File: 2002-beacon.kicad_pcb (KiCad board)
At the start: 2 copper layers, 38.1 x 41.3 mm, 16 parts, among them J3 Barrel_Jack, Q1 2N3904, SW1 SW_SPST, U1 L7805, U2 ATtiny85-20PU

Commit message: fixed routing
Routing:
- net Net-(C1-Pad1): track 7.66 -> 14.0 mm
- net Net-(R2-Pad2): track 29.4 -> 25.7 mm
- net GND: track 0.00 -> 3.60 mm
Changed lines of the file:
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@@
     (thickness 1.6)
     (drawings 5)
-    (tracks 40)
+    (tracks 45)
     (zones 0)
     (modules 16)
@@
   (gr_line (start 128.905 95.885) (end 128.905 54.61) (layer Edge.Cuts) (width 0.05))
   (gr_line (start 91.44 95.885) (end 128.905 95.885) (layer Edge.Cuts) (width 0.05))
-  (segment (start 110.5536 72.39) (end 111.76 72.39) (width 0.4064) (layer F.Cu) (net 1))
-  (segment (start 108.7836 72.39) (end 110.5536 72.39) (width 0.4064) (layer F.Cu) (net 1))
-  (segment (start 106.68 70.2864) (end 108.7836 72.39) (width 0.4064) (layer F.Cu) (net 1))
-  (segment (start 106.68 68.58) (end 106.68 70.2864) (width 0.4064) (layer F.Cu) (net 1))
+  (segment (start 110.5536 72.39) (end 111.76 72.39) (width 0.8) (layer F.Cu) (net 1))
+  (segment (start 108.7836 72.39) (end 110.5536 72.39) (width 0.8) (layer F.Cu) (net 1))
+  (segment (start 106.68 70.2864) (end 108.7836 72.39) (width 0.8) (layer F.Cu) (net 1))
+  (segment (start 106.68 68.58) (end 106.68 70.2864) (width 0.8) (layer F.Cu) (net 1))
+  (segment (start 111.76 72.39) (end 111.76 78.74) (width 0.8) (layer F.Cu) (net 1))
+  (segment (start 113.76 71.25863) (end 113.284 70.78263) (width 0.5) (layer F.Cu) (net 2))
+  (segment (start 113.76 72.39) (end 113.76 71.25863) (width 0.5) (layer F.Cu) (net 2))
+  (segment (start 113.76 73.52137) (end 113.792 73.55337) (width 0.5) (layer F.Cu) (net 2))
+  (segment (start 113.76 72.39) (end 113.76 73.52137) (width 0.5) (layer F.Cu) (net 2))
+  (segment (start 113.76 73.52137) (end 113.76 74.136) (width 0.5) (layer F.Cu) (net 2))
   (segment (start 111.76 88.9636) (end 111.76 83.82) (width 0.8) (layer F.Cu) (net 3))
   (segment (start 111.76 90.17) (end 111.76 88.9636) (width 0.8) (layer F.Cu) (net 3))
@@
   (segment (start 120.65 75.565) (end 118.11 73.025) (width 0.4064) (layer F.Cu) (net 8))
   (segment (start 120.65 78.105) (end 120.65 75.565) (width 0.4064) (layer F.Cu) (net 8))
-  (segment (start 114.963201 80.038201) (end 114.963201 77.498201) (width 0.4064) (layer F.Cu) (net 9))
-  (segment (start 104.775 64.77) (end 107.315 62.23) (width 0.4064) (layer F.Cu) (net 9))
-  (segment (start 118.11 83.185) (end 114.963201 80.038201) (width 0.4064) (layer F.Cu) (net 9))
-  (segment (start 114.963201 77.498201) (end 113.665 76.2) (width 0.4064) (layer F.Cu) (net 9))
-  (segment (start 113.665 76.2) (end 110.49 76.2) (width 0.4064) (layer F.Cu) (net 9))
-  (segment (start 104.775 70.485) (end 104.775 64.77) (width 0.4064) (layer F.Cu) (net 9))
-  (segment (start 110.49 76.2) (end 104.775 70.485) (width 0.4064) (layer F.Cu) (net 9))
+  (segment (start 114.963201 80.038201) (end 114.963201 77.498201) (width 0.408) (layer F.Cu) (net 9))
+  (segment (start 118.11 83.185) (end 114.963201 80.038201) (width 0.408) (layer F.Cu) (net 9))
+  (segment (start 114.963201 75.028799) (end 115.316 74.676) (width 0.408) (layer F.Cu) (net 9))
+  (segment (start 114.963201 77.498201) (end 114.963201 75.028799) (width 0.408) (layer F.Cu) (net 9))
+  (segment (start 115.316 70.231) (end 107.315 62.23) (width 0.408) (layer F.Cu) (net 9))
+  (segment (start 115.316 74.676) (end 115.316 70.231) (width 0.408) (layer F.Cu) (net 9))
   (segment (start 116.205 78.74) (end 118.11 80.645) (width 0.4064) (layer F.Cu) (net 10))
   (segment (start 116.205 66.04) (end 116.205 78.74) (width 0.4064) (layer F.Cu) (net 10))

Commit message: Layout for rev2 done
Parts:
- removed C2: CP1, Capacitor_THT:CP_Radial_D5.0mm_P2.00mm
- removed J3: Barrel_Jack, Connector_BarrelJack:BarrelJack_CUI_PJ-102AH_Horizontal
- removed U1: L7805, Package_TO_SOT_THT:TO-220-3_Horizontal_TabUp
- added C3: C, Capacitor_THT:CP_Radial_D5.0mm_P2.00mm, F.Cu at (95.0, 77.0)
- added D3: LED, LED_THT:LED_D3.0mm_Horizontal_O3.81mm_Z6.0mm, F.Cu at (104.2, 85.0)
- added J1: USB_B, Connector_USB:USB_Micro-B_Molex-105017-0001, F.Cu at (65.0, 88.0)
- added Q2: 2N3904, Package_TO_SOT_THT:TO-92_Inline, F.Cu at (96.0, 85.0)
- added R4: 74, Resistor_THT:R_Axial_DIN0204_L3.6mm_D1.6mm_P7.62mm_Horizontal, F.Cu at (83.4, 82.0)
- added R5: 470, Resistor_THT:R_Axial_DIN0204_L3.6mm_D1.6mm_P7.62mm_Horizontal, F.Cu at (91.0, 85.0)
- C1: value CP1 -> C
- R3: value 90 -> 74
- moved H2 61.0 mm to (66.0, 77.0)
- moved SW1 52.4 mm to (72.5, 89.0), turned to 0 degrees
- moved H1 46.2 mm to (103.0, 99.0)
- moved U2 46.1 mm to (72.0, 77.0)
- moved D2 45.7 mm to (87.0, 99.0), turned to 0 degrees
- moved R2 40.8 mm to (82.0, 99.0), turned to 180 degrees
- moved R1 40.1 mm to (91.0, 93.0)
- moved R3 39.8 mm to (83.4, 90.0)
- moved Q1 37.0 mm to (96.0, 93.0), turned to 90 degrees
- moved D1 33.5 mm to (104.2, 93.0)
- moved H4 29.4 mm to (66.0, 99.0)
- moved C1 28.1 mm to (84.0, 77.0)
- moved H3 20.4 mm to (103.0, 77.0)
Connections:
- C1 pad 1: Net-(C1-Pad1) -> +5V
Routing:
- net +5V: track 51.9 -> 76.4 mm
- net Net-(D3-Pad1): track 0.00 -> 16.5 mm
- net Net-(C1-Pad1): track 14.0 -> 0.00 mm
- net Net-(Q2-Pad3): track 0.00 -> 13.5 mm
- net Net-(D1-Pad1): track 3.17 -> 15.9 mm
- net Net-(R1-Pad2): track 13.3 -> 23.3 mm
- net Net-(Q1-Pad3): track 5.08 -> 13.4 mm
- net Net-(SW1-Pad1): track 20.7 -> 13.6 mm
- net Net-(R2-Pad2): track 25.7 -> 19.5 mm
- net Net-(Q1-Pad2): track 11.4 -> 5.53 mm
- net Net-(Q2-Pad2): track 0.00 -> 5.53 mm
- net Net-(D2-Pad2): track 6.40 -> 9.24 mm
- net GND: track 3.60 -> 6.04 mm, vias 0 -> 2
- added copper zone on F.Cu, net +5V
- added copper zone on B.Cu, net GND
- removed copper zone on F.Cu, net GND
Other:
- board size 38.1 x 41.3 mm -> 45 x 30 mm

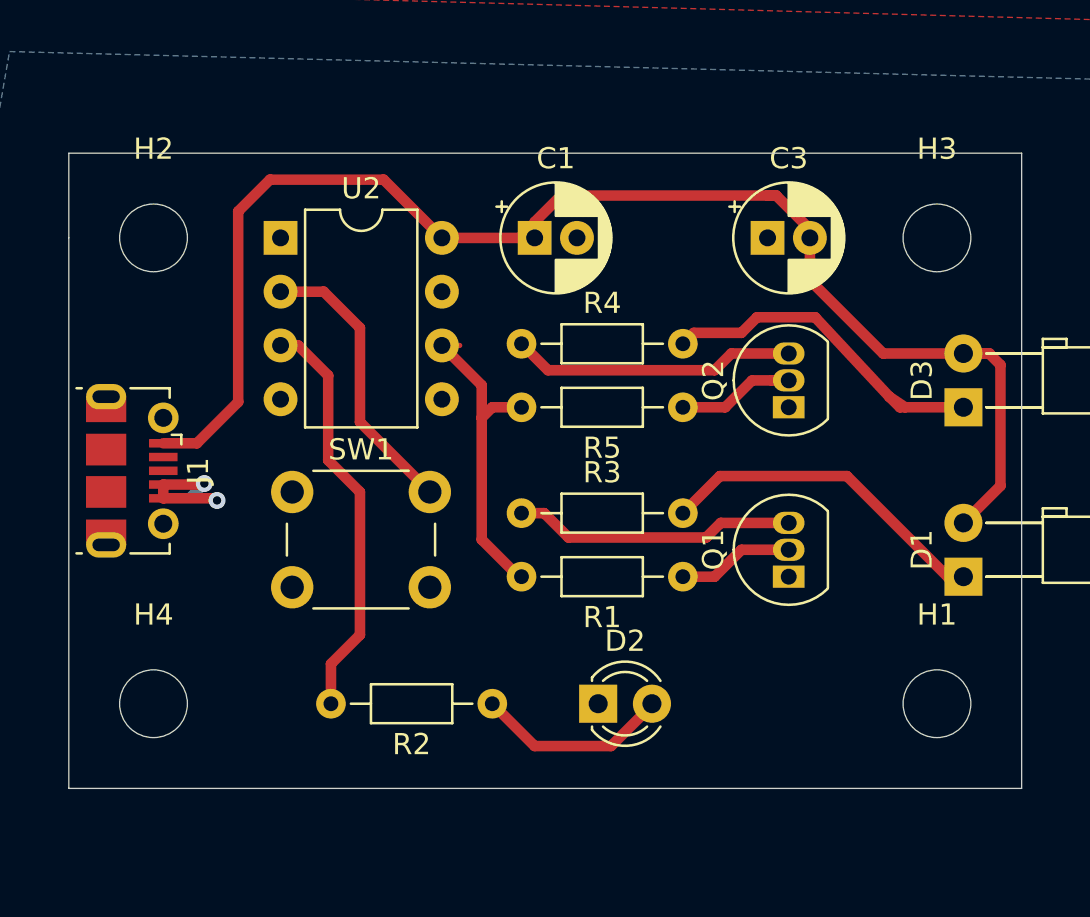
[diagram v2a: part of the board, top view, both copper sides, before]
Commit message: some cleanup of traces, clenup silk, add board ver and authors
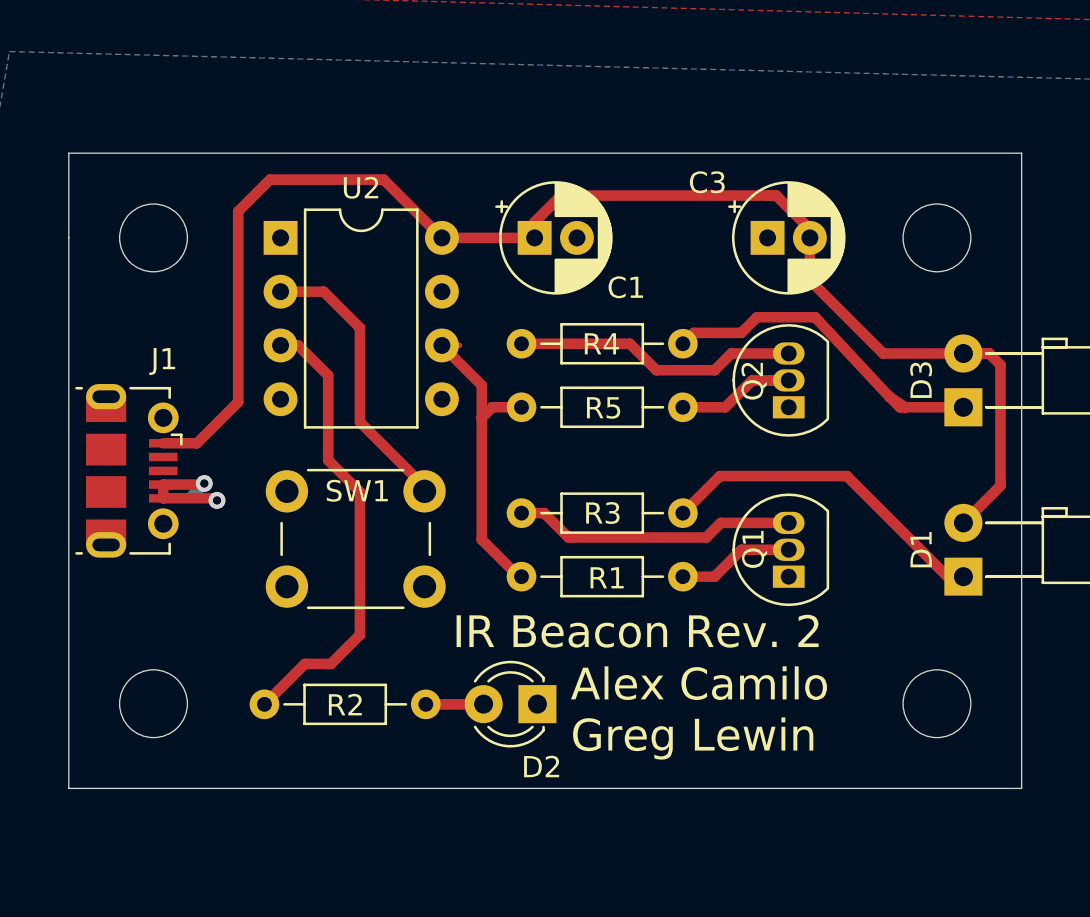
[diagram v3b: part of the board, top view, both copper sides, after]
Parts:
- moved R2 3.14 mm to (78.9, 99.0)
- moved D2 2.87 mm to (84.1, 99.0), turned to 180 degrees
- moved SW1 0.25 mm to (72.3, 89.0)
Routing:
- net Net-(D2-Pad2): track 9.24 -> 2.73 mm
- net Net-(R2-Pad2): track 19.5 -> 21.6 mm
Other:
- board text added: "Alex Camilo Greg Lewin"
- board text added: "IR Beacon Rev. 2"
